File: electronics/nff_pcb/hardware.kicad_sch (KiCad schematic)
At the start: 20 parts, among them J1 Micro_SD_Card_Det_Hirose_DM3AT, J10 Power Select, J2 USB_A, J3 USB_A, J4 Conn_01x08_Pin, J5 USB_C_Receptacle_USB2.0_16P, J6 Conn_01x10_Pin

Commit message: R0.1 released.
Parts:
- C94: MPN GRM155R60J226ME11D -> GRM158R60J226ME01D
- J10: now left out of the parts list
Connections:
- net SD_CLK renamed SDC0.CLK
- net SD_CMD renamed SDC0.CMD
- net SD_DAT0 renamed SDC0.D0
- net SD_DAT1 renamed SDC0.D1
- net SD_DAT2 renamed SDC0.D2
- net SD_DAT3 renamed SDC0.D3
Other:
- sheet A33_GPIO ports: added {SDC0}, {SDC1}; removed SD_CLK, SD_CMD, SD_DAT[0..3], {SDC}
- sheet WiFi ports: added {SDC1}; removed {SDC}
- moved on the sheet: J10

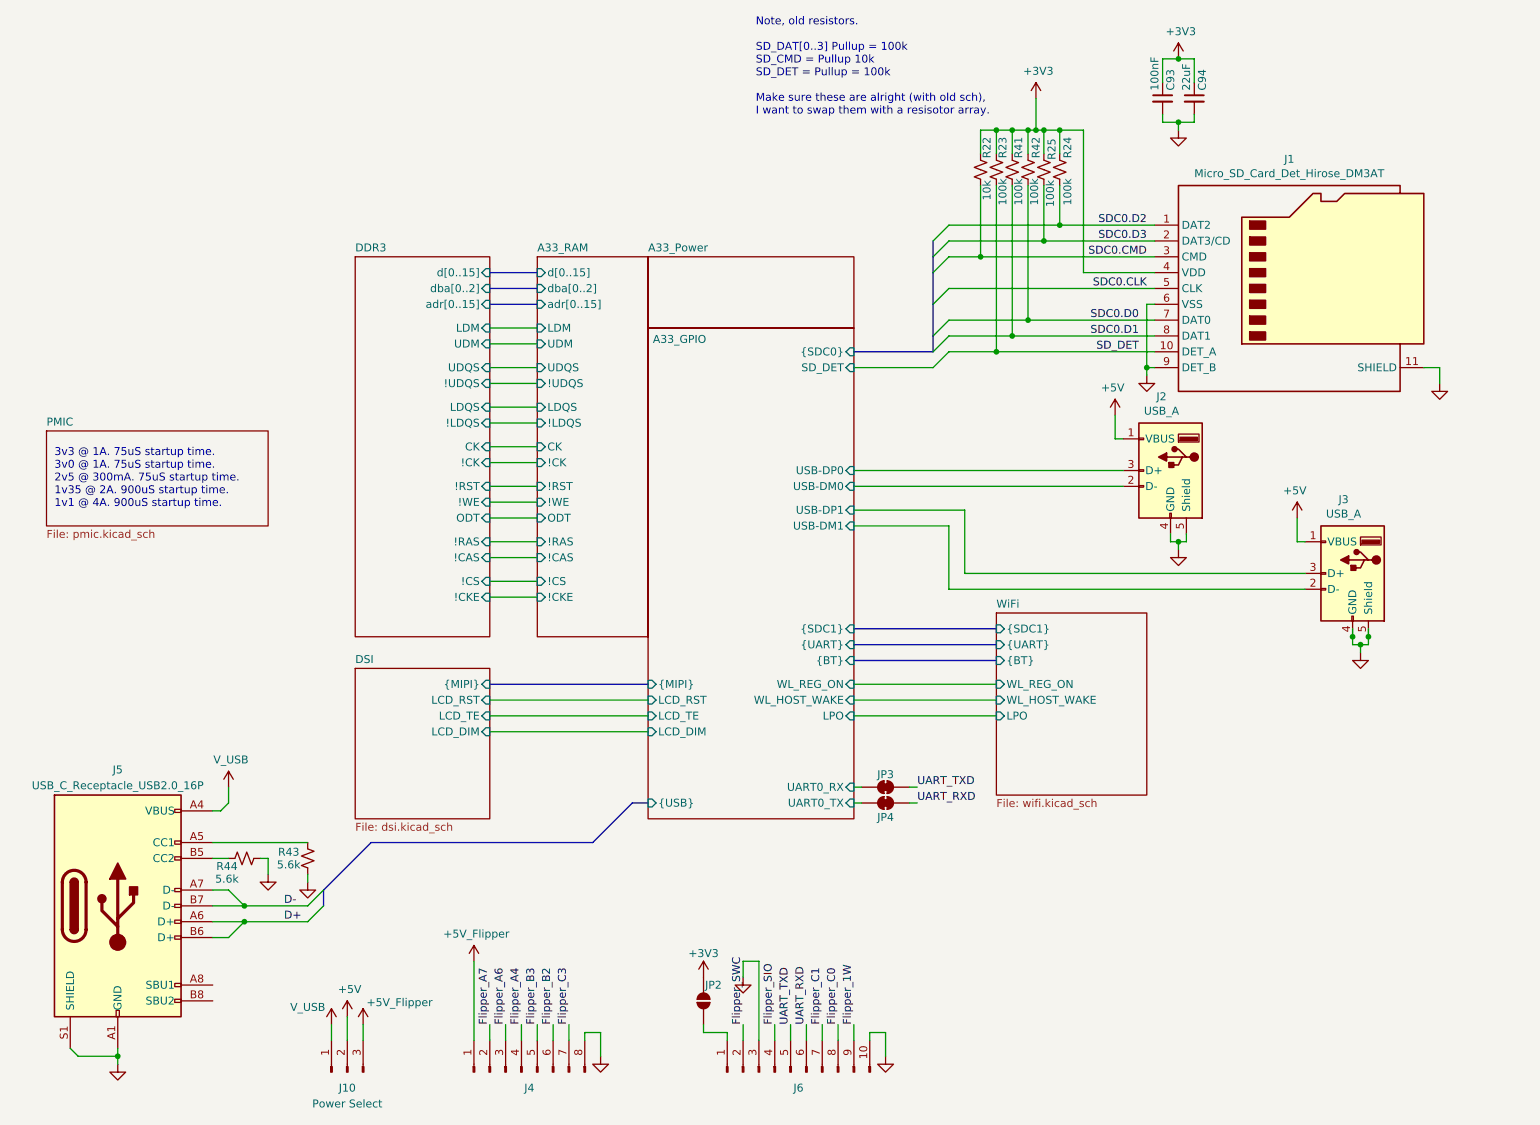
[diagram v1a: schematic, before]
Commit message: “or” the 5V line, “or” the UART bus, reroute the PWM line to be actually PWM, Reset button., Decoup caps over USB.
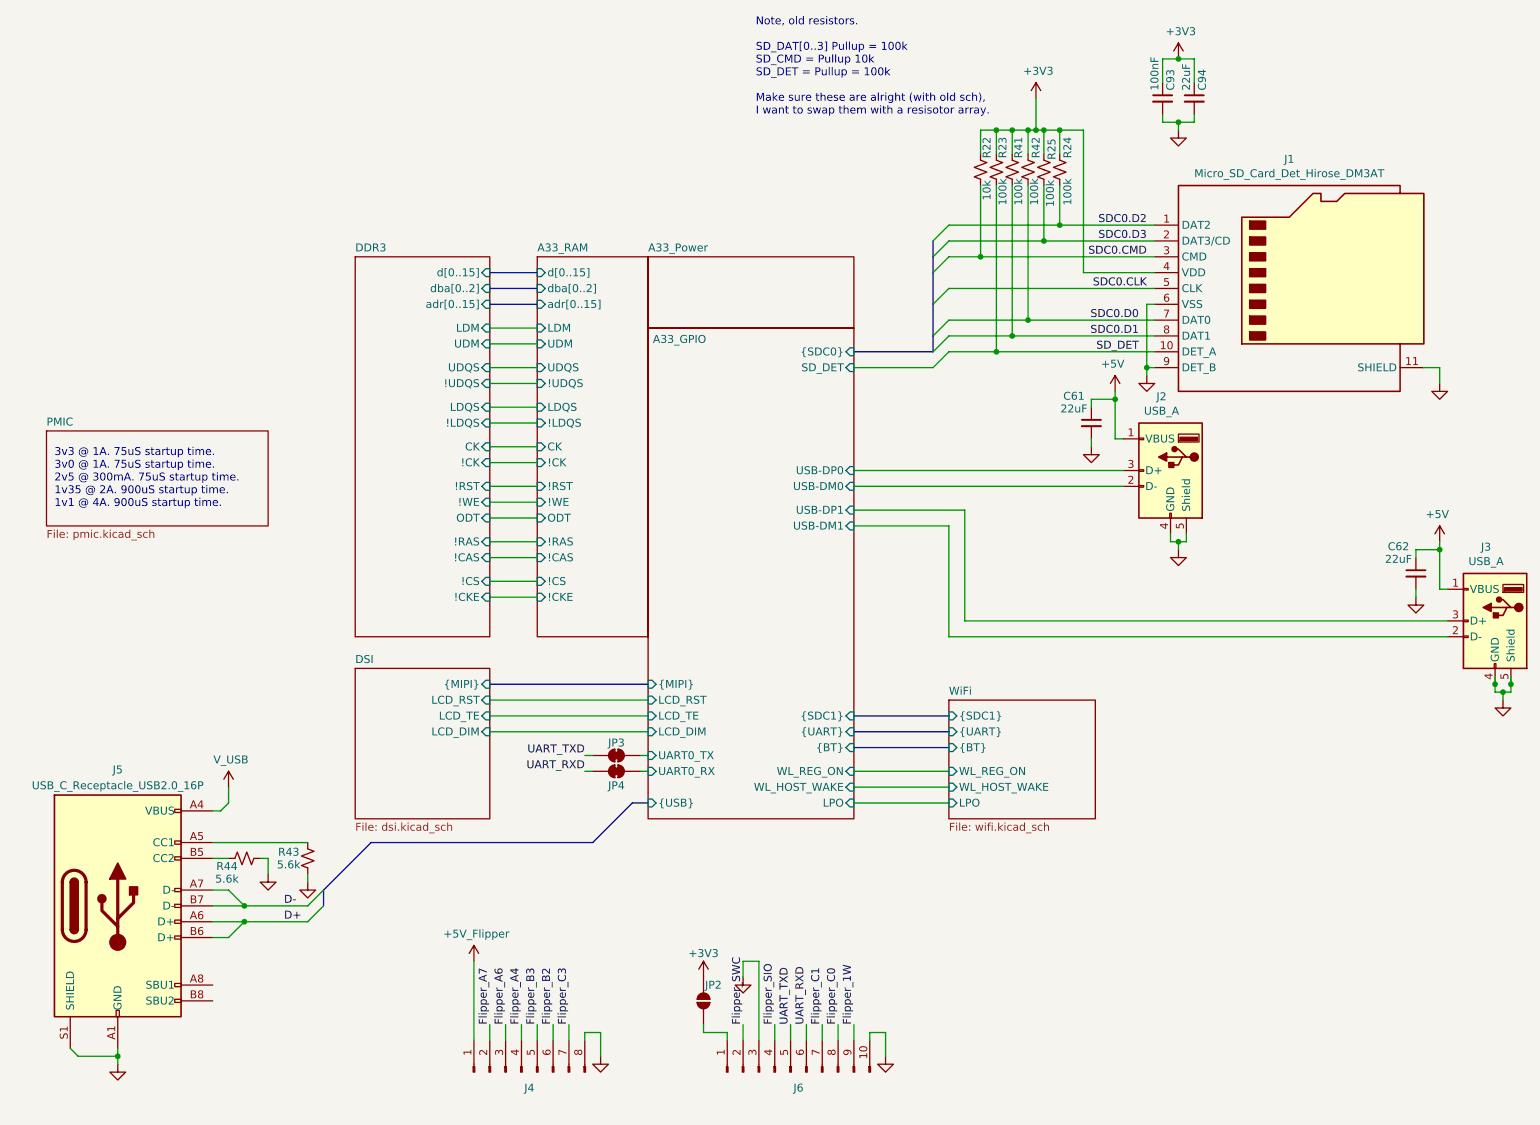
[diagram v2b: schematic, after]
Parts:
- removed J10: Power Select, Connector_PinHeader_2.54mm:PinHeader_1x03_P2.54mm_Vertical, symbol Connector:Conn_01x03_Pin
- added C61, C62: 22uF, Capacitor_SMD:C_0402_1005Metric, symbol Device:C_Small
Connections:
- net +5V: now also C61.1, C62.1
- net A33_GPIO/UART0_RX: now also JP4.1 (A); no longer JP3.1 (A)
- net A33_GPIO/UART0_TX: now also JP3.1 (A); no longer JP4.1 (A)
- net GND: now also C61.2, C62.2
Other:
- moved on the sheet: J3, JP3, JP4

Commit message: R2 Released
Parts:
- added U14, U15: NUP2202, Package_TO_SOT_SMD:SOT-363_SC-70-6, symbol Power_Protection:NUP2202
- R22: MPN RC0402FR-1310KL -> RC0402JR-0710KL
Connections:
- net +5V: now also U14.5, U15.5
- net A33_GPIO/USB-DM0: now also U14.6
- net A33_GPIO/USB-DM1: now also U15.6
- net A33_GPIO/USB-DP0: now also U14.1
- net A33_GPIO/USB-DP1: now also U15.1
- net GND: now also U14.2, U15.2
